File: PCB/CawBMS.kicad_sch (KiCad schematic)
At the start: 37 parts, among them CN1 SWD, CN2 I2C, CN3 SPI, CN4 USART, CN5 SWD, SW1 B3U-1000P, SW2 B3U-1000P, U1 STM32F103CBTx, U2 TCAN1044DRBRQ1, U5 CAN, X1 Crystal_16MHz_15pF_3P

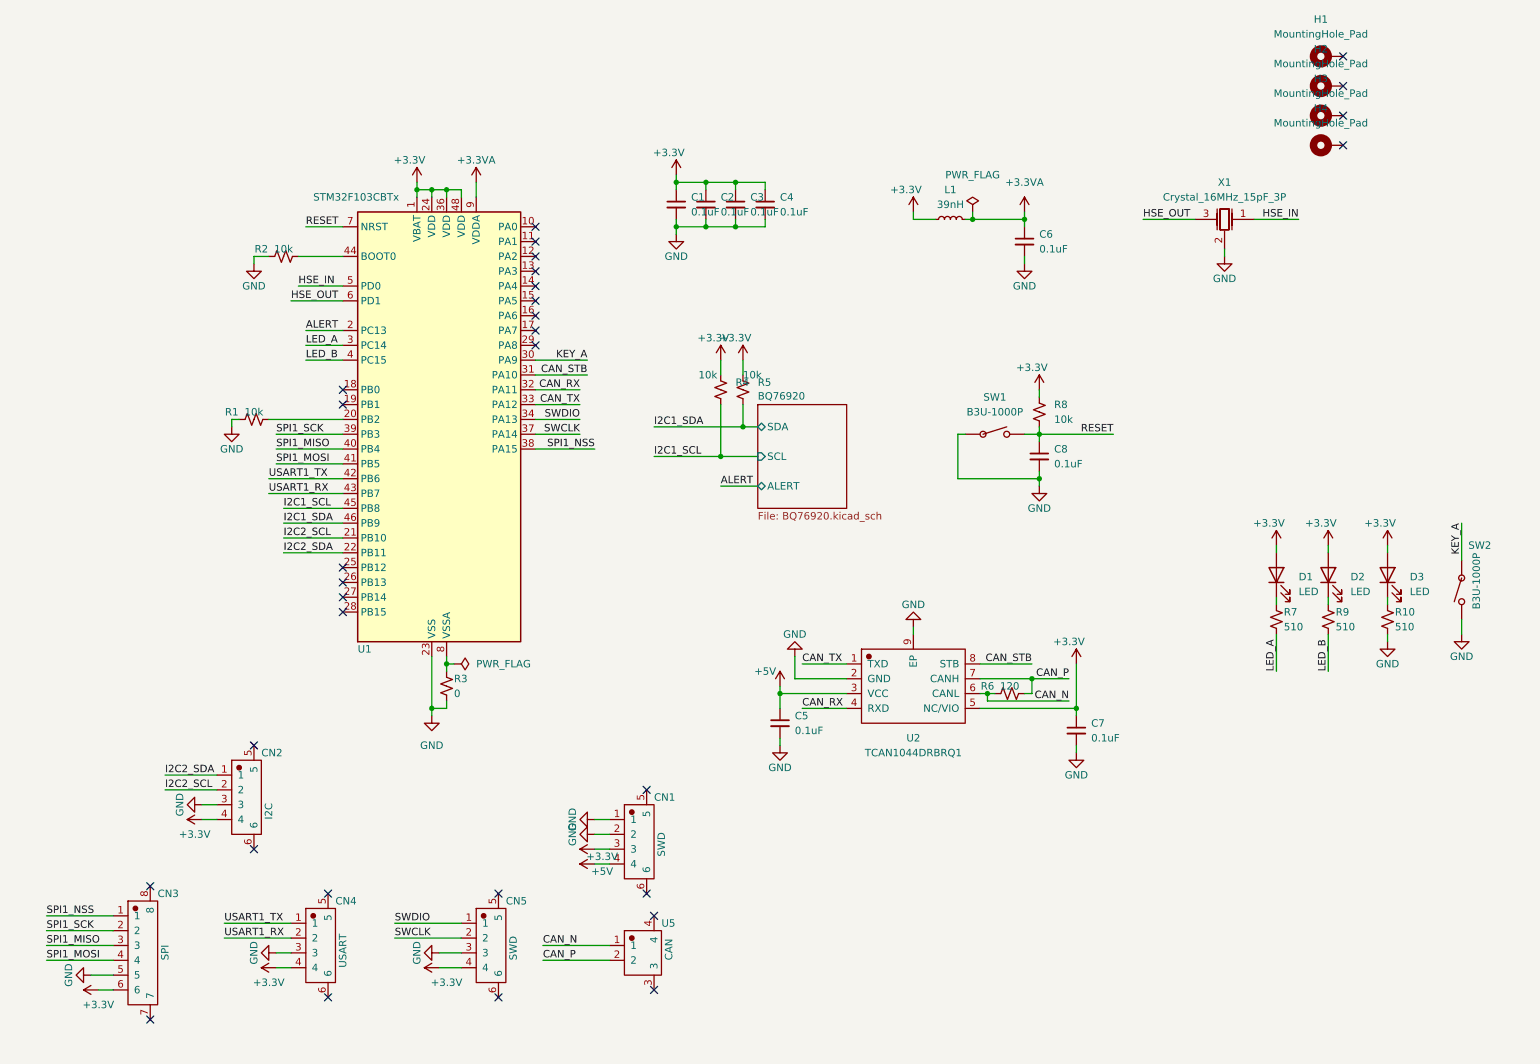
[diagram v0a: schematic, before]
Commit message: feat(PCB): 新增预充功能; 支持2路电池温度采样; 支持低功耗模式; 更换主控芯片; 采用降压输出5V
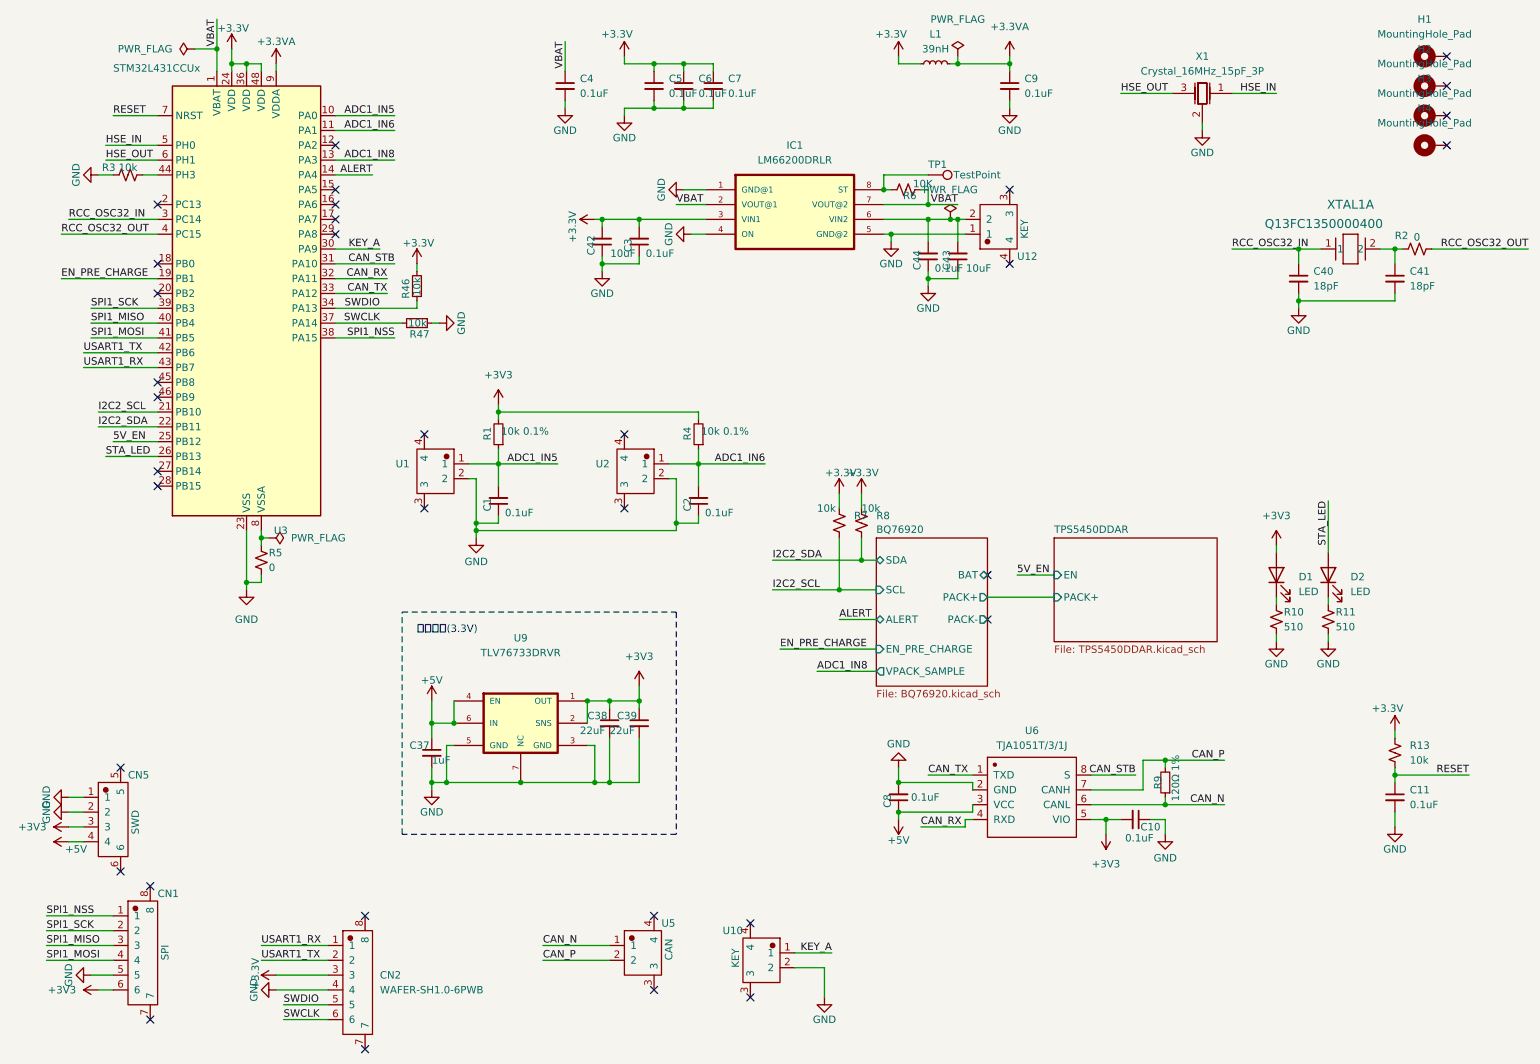
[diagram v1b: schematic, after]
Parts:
- removed C5, C7: 0.1uF, Capacitor_SMD:C_0402_1005Metric_Pad0.74x0.62mm_HandSolder, symbol Device:C_Small
- removed CN2: I2C, Rick_Connector:CONN-SMD_4P-P1.00_WAFER-SH1.0-4PWB, symbol Rick_Connector:WAFER-SH1.0-4PWB
- removed CN4: USART, Rick_Connector:CONN-SMD_4P-P1.00_WAFER-SH1.0-4PWB, symbol Rick_Connector:WAFER-SH1.0-4PWB
- removed CN5: SWD, Rick_Connector:CONN-SMD_4P-P1.00_WAFER-SH1.0-4PWB, symbol Rick_Connector:WAFER-SH1.0-4PWB
- removed D3: LED, LED_SMD:LED_0402_1005Metric_Pad0.77x0.64mm_HandSolder, symbol Device:LED
- removed R1: 10k, Resistor_SMD:R_0402_1005Metric_Pad0.72x0.64mm_HandSolder, symbol Device:R_Small_US
- removed R10: 510, Resistor_SMD:R_0402_1005Metric_Pad0.72x0.64mm_HandSolder, symbol Device:R_Small_US
- removed R6: 120, Resistor_SMD:R_0402_1005Metric_Pad0.72x0.64mm_HandSolder, symbol Device:R_Small_US
- removed SW1, SW2: B3U-1000P, Rick_Switch:B3U-1000P, symbol Rick_Switch:B3U-1000P
- removed U1: STM32F103CBTx, Package_QFP:LQFP-48_7x7mm_P0.5mm, symbol MCU_ST_STM32F1:STM32F103CBTx
- removed U2: TCAN1044DRBRQ1, Rick_CAN:TCAN1044DRBRQ1_DFN-8_L3.0-W3.0-P0.65-TL-EP2.4, symbol Rick_CAN:TCAN1044DRBRQ1
- added C1, C10, C2, C3, C44, C8: 0.1uF, Capacitor_SMD:C_0402_1005Metric_Pad0.74x0.62mm_HandSolder, symbol Library:C_Small
- added C37: 1uF, Capacitor_SMD:C_0402_1005Metric_Pad0.74x0.62mm_HandSolder, symbol Library:C_Small
- added C38, C39: 22uF, Capacitor_SMD:C_0603_1608Metric_Pad1.08x0.95mm_HandSolder, symbol Library:C_Small
- added C40, C41: 18pF, Capacitor_SMD:C_0402_1005Metric_Pad0.74x0.62mm_HandSolder, symbol Library:C_Small
- added C42, C43: 10uF, Capacitor_SMD:C_0402_1005Metric_Pad0.74x0.62mm_HandSolder, symbol Library:C_Small
- added CN2: WAFER-SH1.0-6PWB, Rick_Connector:CONN-SMD_6P-P1.00_XUNPU_WAFER-SH1.0-6PWB, symbol Library:WAFER-SH1.0-6PWB
- added IC1: LM66200DRLR, Rick_Diode:LM66200DRLR, symbol Library:LM66200DRLR
- added R1, R4: 10k 0.1%, Resistor_SMD:R_0402_1005Metric_Pad0.72x0.64mm_HandSolder, symbol Library:R_Small
- added R2: 0, Resistor_SMD:R_0402_1005Metric_Pad0.72x0.64mm_HandSolder, symbol Library:R_Small_US
- added R46, R47: 10k, Resistor_SMD:R_0402_1005Metric_Pad0.72x0.64mm_HandSolder, symbol Library:R_Small
- added R6: 10K, Resistor_SMD:R_0402_1005Metric_Pad0.72x0.64mm_HandSolder, symbol Library:R_Small_US
- added R9: 120Ω 1%, Resistor_SMD:R_0402_1005Metric_Pad0.72x0.64mm_HandSolder, symbol Library:R_Small
- added TP1: TestPoint, TestPoint:TestPoint_Pad_D1.0mm, symbol Library:TestPoint
- added U1, U2: WAFER-SH1.0-2PWB, Rick_Connector:CONN-SMD_2P-P1.00_XUNPU_WAFER-SH1.0-2PWB, symbol Library:WAFER-SH1.0-2PWB
- added U10, U12: KEY, Rick_Connector:CONN-SMD_2P-P1.00_XUNPU_WAFER-SH1.0-2PWB, symbol Library:WAFER-SH1.0-2PWB
- added U3: STM32L431CCUx, Package_DFN_QFN:QFN-48-1EP_7x7mm_P0.5mm_EP5.6x5.6mm, symbol Library:STM32L431CCUx
- added U6: TJA1051T/3/1J, Rick_CAN:TJA1051T31J_SOIC-8_L4.9-W3.9-P1.27-LS6.0-BL, symbol Library:TJA1051T/3/1J
- added U9: TLV76733DRVR, Rick_Regulator_Linear:TLV76733DRVR_SON65P200X200X80-7N, symbol Library:TLV76733DRVR
- added XTAL1: Q13FC1350000400, Rick_Crystal:Q13FC1350000400, symbol Library:Q13FC1350000400
- C11: renamed from C8; symbol Device:C_Small -> Library:C_Small
- C4: renamed from C1; symbol Device:C_Small -> Library:C_Small
- C5: renamed from C2; symbol Device:C_Small -> Library:C_Small
- C6: renamed from C3; symbol Device:C_Small -> Library:C_Small
- C7: renamed from C4; symbol Device:C_Small -> Library:C_Small
- C9: renamed from C6; symbol Device:C_Small -> Library:C_Small
- CN1: renamed from CN3; symbol Rick_Connector:WAFER-SH1.0-6PWB -> Library:WAFER-SH1.0-6PWB
- CN5: renamed from CN1; symbol Rick_Connector:WAFER-SH1.0-4PWB -> Library:WAFER-SH1.0-4PWB
- D1, D2: symbol Device:LED -> Library:LED
- H1, H2, H3, H4: symbol Mechanical:MountingHole_Pad -> Library:MountingHole_Pad
- L1: symbol Device:L_Small -> Library:L_Small
- R10: renamed from R7; symbol Device:R_Small_US -> Library:R_Small_US
- R11: renamed from R9; symbol Device:R_Small_US -> Library:R_Small_US
- R13: renamed from R8; symbol Device:R_Small_US -> Library:R_Small_US
- R3: renamed from R2; symbol Device:R_Small_US -> Library:R_Small_US
- R5: renamed from R3; symbol Device:R_Small_US -> Library:R_Small_US
- R7: renamed from R4; symbol Device:R_Small_US -> Library:R_Small_US
- R8: renamed from R5; symbol Device:R_Small_US -> Library:R_Small_US
- U5: symbol Rick_Connector:WAFER-SH1.0-2PWB -> Library:WAFER-SH1.0-2PWB
- X1: symbol Rick_Device:Crystal_16MHz_15pF_3P -> Library:Crystal_16MHz_15pF_3P
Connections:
- net I2C1_SCL is gone; now on net I2C2_SCL: R7.2
- net I2C1_SDA is gone; now on net I2C2_SDA: R8.2
- net LED_A is gone; now on net GND: R10.2
- net LED_B is gone; now on net GND: R11.2
- net +3.3V: now also C3.2, C42.2, CN2.3, IC1.3 (VIN1), R46.2, U3.24 (VDD), U3.36 (VDD), U3.48 (VDD); no longer C4.1, CN1.6, CN5.3, D1.2 (A), D2.2 (A)
- net +3.3VA: now also U3.9 (VDDA)
- net +5V: now also C37.1, C8.1, U6.3 (VCC), U9.4 (EN), U9.6 (IN)
- net ALERT: now also U3.14 (PA4)
- net CAN_N: now also R9.1, U6.6 (CANL)
- net CAN_P: now also R9.2, U6.7 (CANH)
- net CAN_RX: now also U3.32 (PA11), U6.4 (RXD)
- net CAN_STB: now also U3.31 (PA10), U6.8 (S)
- net CAN_TX: now also U3.33 (PA12), U6.1 (TXD)
- net GND: now also C1.1, C10.1, C2.1, C3.1, C37.2, C38.2, C39.2, C40.2, C41.2, C42.1, C43.1, C44.1, C8.2, CN2.4, IC1.1 (GND@1), IC1.4 (ON), IC1.5 (GND@2), R47.1, U1.2, U10.2, U12.1, U2.2, U3.23 (VSS), U3.35 (VSS), U3.47 (VSS), U3.49 (VSS), U6.2 (GND), U9.3 (GND), U9.5 (GND), U9.7 (NC)
- net HSE_IN: now also U3.5 (PH0)
- net HSE_OUT: now also U3.6 (PH1)
- net I2C2_SCL: now also U3.21 (PB10)
- net I2C2_SDA: now also U3.22 (PB11)
- net KEY_A: now also U10.1, U3.30 (PA9)
- net RESET: now also U3.7 (NRST)
- net SPI1_MISO: now also U3.40 (PB4)
- net SPI1_MOSI: now also U3.41 (PB5)
- net SPI1_NSS: now also U3.38 (PA15)
- net SPI1_SCK: now also U3.39 (PB3)
- net SWCLK: now also CN2.6, R47.2, U3.37 (PA14)
- net SWDIO: now also CN2.5, R46.1, U3.34 (PA13)
- net USART1_RX: now also CN2.1, U3.43 (PB7)
- net USART1_TX: now also CN2.2, U3.42 (PB6)
- net at R5.1: now also U3.8 (VSSA)
- net at R3.2: now also U3.44 (PH3)
- new net: C43.2, C44.2, IC1.6 (VIN2), U12.2
- new net: C41.1, R2.1, XTAL1.2
- new net: IC1.8 (ST), R6.1, TP1.1
- new net +3V3: C10.2, C38.1, C39.1, CN1.6, CN5.3, D1.2 (A), R1.2, R4.2, U6.5 (VIO), U9.1 (OUT), U9.2 (SNS)
- new net 5V_EN: U3.25 (PB12)
- new net ADC1_IN5: C1.2, R1.1, U1.1, U3.10 (PA0)
- new net ADC1_IN6: C2.2, R4.1, U2.1, U3.11 (PA1)
- new net ADC1_IN8: U3.13 (PA3)
- new net EN_PRE_CHARGE: U3.19 (PB1)
- new net RCC_OSC32_IN: C40.1, U3.3 (PC14), XTAL1.1
- new net RCC_OSC32_OUT: R2.2, U3.4 (PC15)
- new net STA_LED: D2.2 (A), U3.26 (PB13)
- new net VBAT: C4.1, IC1.2 (VOUT@1), IC1.7 (VOUT@2), R6.2, U3.1 (VBAT)
- no-connect marks 31 -> 34
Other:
- added sheet TPS5450DDAR (TPS5450DDAR.kicad_sch)
- sheet BQ76920 ports: added BAT, EN_PRE_CHARGE, PACK+, PACK-, VPACK_SAMPLE; removed none
- note added: "降压电路(3.3V)"
- moved on the sheet: C11, C4, C5, C6, C7, C9, CN5, H1, H2, H3, H4, L1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
